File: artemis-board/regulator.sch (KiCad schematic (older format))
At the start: 33 parts, among them Q5 AO3401A, Q6 AO3401A, Q7 2N7002, Q8 2N7002, Q9 AO3401A, U10 FP6291LR, U11 ME6210A33P, U12 ME6210A33P

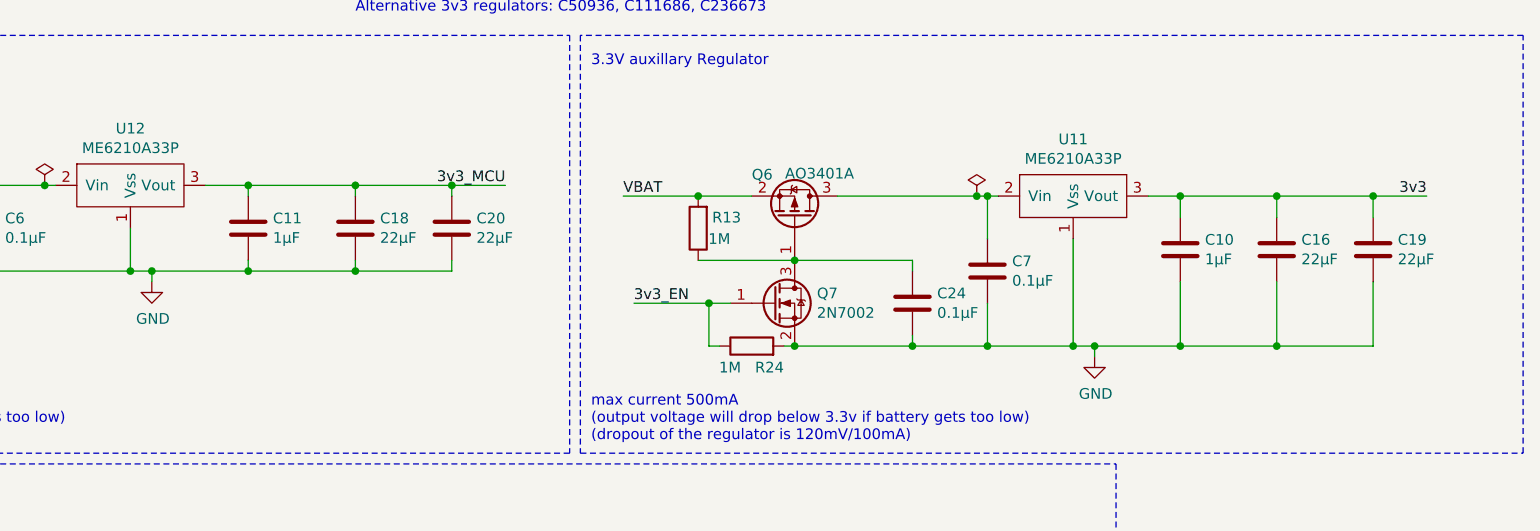
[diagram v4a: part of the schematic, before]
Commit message: removed unprotected connector, added jumper, moved cap to 3v3_mcu
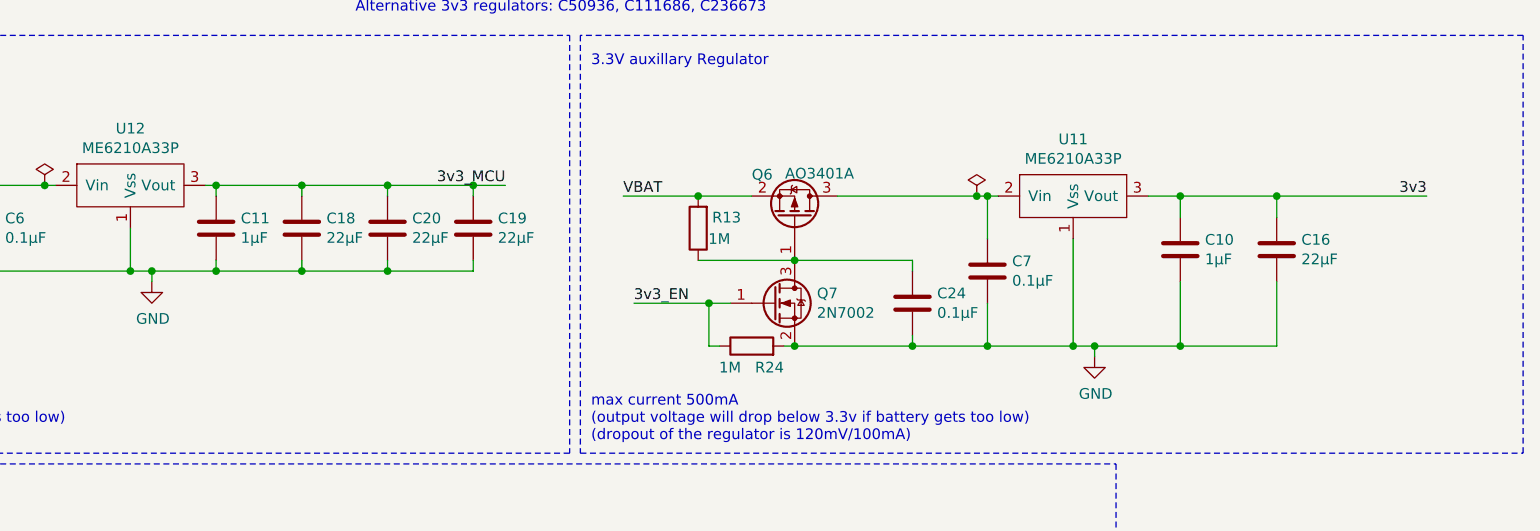
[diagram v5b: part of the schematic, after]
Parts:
- U11, U12: footprint Package_TO_SOT_SMD:SOT-89-3_Handsoldering -> Package_TO_SOT_SMD:SOT-89-3
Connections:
- net 3v3: no longer C19.1
- net 3v3_MCU: now also C19.1
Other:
- moved on the sheet: C11, C18, C20
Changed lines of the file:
@@
 VBAT
-Wire Wire Line
-	8950 3050 9400 3050
 Wire Wire Line
 	5950 3550 6300 3550
@@
 	2700 3000 2900 3000
 Wire Wire Line
-	3950 3000 4150 3000
-Wire Wire Line
-	4650 3050 4650 3000
-Connection ~ 4650 3000
-Wire Wire Line
-	4150 3050 4150 3000
-Connection ~ 4150 3000
-Wire Wire Line
-	4150 3000 4650 3000
-Wire Wire Line
-	4650 3350 4650 3400
-Wire Wire Line
-	4650 3400 4150 3400
-Wire Wire Line
-	4150 3400 4150 3350
-Connection ~ 4150 3400
+	3950 3000 4000 3000
+Wire Wire Line
+	4400 3050 4400 3000
+Wire Wire Line
+	4000 3050 4000 3000
+Wire Wire Line
+	4400 3350 4400 3400
+Wire Wire Line
+	4000 3400 4000 3350
 Connection ~ 3600 3400
 Wire Wire Line
@@
 Connection ~ 3700 3400
 Wire Wire Line
-	3700 3400 4150 3400
+	3700 3400 4000 3400
 Wire Wire Line
 	8100 3800 8100 3750
@@
 	600  600  600  2050
 Wire Wire Line
-	9400 3450 9400 3750
-Wire Wire Line
-	5100 3350 5100 3400
-Wire Wire Line
-	5100 3400 4650 3400
-Connection ~ 4650 3400
-Wire Wire Line
-	5100 3050 5100 3000
-Wire Wire Line
-	4650 3000 5100 3000
+	4800 3350 4800 3400
+Wire Wire Line
+	4800 3050 4800 3000
 Text Label 5350 3000 2    50   ~ 0
 3v3_MCU
-Wire Wire Line
-	5350 3000 5100 3000
-Connection ~ 5100 3000
-Wire Wire Line
-	8950 3750 9400 3750
-Connection ~ 8950 3750
-Wire Wire Line
-	9400 3150 9400 3050
-Connection ~ 9400 3050
-Wire Wire Line
-	9400 3050 9650 3050
 Wire Notes Line
 	1200 4300 8200 4300
@@
 L Device:C C20
 U 1 1 6037883A
-P 5100 3200
-F 0 "C20" H 5215 3246 50  0000 L CNN
-F 1 "22µF" H 5215 3155 50  0000 L CNN
-F 2 "Capacitor_SMD:C_0805_2012Metric" H 5138 3050 50  0001 C CNN
-F 3 "~" H 5100 3200 50  0001 C CNN
-F 4 "C45783" H 5100 3200 50  0001 C CNN "LCSC"
-	1    5100 3200
-	1    0    0    -1
-$EndComp
-$Comp
-L Device:C C19
-U 1 1 60374573
-P 9400 3300
-F 0 "C19" H 9515 3346 50  0000 L CNN
-F 1 "22µF" H 9515 3255 50  0000 L CNN
-F 2 "Capacitor_SMD:C_0805_2012Metric" H 9438 3150 50  0001 C CNN
-F 3 "~" H 9400 3300 50  0001 C CNN
-F 4 "C45783" H 9400 3300 50  0001 C CNN "LCSC"
-	1    9400 3300
+P 4800 3200
+F 0 "C20" H 4915 3246 50  0000 L CNN
+F 1 "22µF" H 4915 3155 50  0000 L CNN
+F 2 "Capacitor_SMD:C_0805_2012Metric" H 4838 3050 50  0001 C CNN
+F 3 "~" H 4800 3200 50  0001 C CNN
+F 4 "C45783" H 4800 3200 50  0001 C CNN "LCSC"
+	1    4800 3200
 	1    0    0    -1
 $EndComp
@@
 F 0 "U12" H 3600 3265 50  0000 C CNN
 F 1 "ME6210A33P" H 3600 3174 50  0000 C CNN
-F 2 "Package_TO_SOT_SMD:SOT-89-3_Handsoldering" H 3600 3450 50  0001 C CNN
+F 2 "Package_TO_SOT_SMD:SOT-89-3" H 3600 3450 50  0001 C CNN
 F 3 "https://datasheet.lcsc.com/szlcsc/1810201611_MICRONE-Nanjing-Micro-One-Elec-ME6210A33PG_C85233.pdf" H 3600 3450 50  0001 C CNN
 F 4 "C85233" H 3600 3550 50  0001 C CNN "LCSC"
@@
 L Device:C C18
 U 1 1 5F87C4EA
-P 4650 3200
-F 0 "C18" H 4765 3246 50  0000 L CNN
-F 1 "22µF" H 4765 3155 50  0000 L CNN
-F 2 "Capacitor_SMD:C_0805_2012Metric" H 4688 3050 50  0001 C CNN
-F 3 "~" H 4650 3200 50  0001 C CNN
-F 4 "C45783" H 4650 3200 50  0001 C CNN "LCSC"
-	1    4650 3200
+P 4400 3200
+F 0 "C18" H 4515 3246 50  0000 L CNN
+F 1 "22µF" H 4515 3155 50  0000 L CNN
+F 2 "Capacitor_SMD:C_0805_2012Metric" H 4438 3050 50  0001 C CNN
+F 3 "~" H 4400 3200 50  0001 C CNN
+F 4 "C45783" H 4400 3200 50  0001 C CNN "LCSC"
+	1    4400 3200
 	1    0    0    -1
 $EndComp
@@
 L Device:C C11
 U 1 1 5F822A09
-P 4150 3200
-F 0 "C11" H 4265 3246 50  0000 L CNN
-F 1 "1µF" H 4265 3155 50  0000 L CNN
-F 2 "Capacitor_SMD:C_0603_1608Metric_Pad1.08x0.95mm_HandSolder" H 4188 3050 50  0001 C CNN
-F 3 "~" H 4150 3200 50  0001 C CNN
-F 4 "C15849" H 4150 3200 50  0001 C CNN "LCSC"
-	1    4150 3200
+P 4000 3200
+F 0 "C11" H 4115 3246 50  0000 L CNN
+F 1 "1µF" H 4115 3155 50  0000 L CNN
+F 2 "Capacitor_SMD:C_0603_1608Metric_Pad1.08x0.95mm_HandSolder" H 4038 3050 50  0001 C CNN
+F 3 "~" H 4000 3200 50  0001 C CNN
+F 4 "C15849" H 4000 3200 50  0001 C CNN "LCSC"
+	1    4000 3200
 	1    0    0    -1
 $EndComp
@@
 F 0 "U11" H 8000 3315 50  0000 C CNN
 F 1 "ME6210A33P" H 8000 3224 50  0000 C CNN
-F 2 "Package_TO_SOT_SMD:SOT-89-3_Handsoldering" H 8000 3500 50  0001 C CNN
+F 2 "Package_TO_SOT_SMD:SOT-89-3" H 8000 3500 50  0001 C CNN
 F 3 "https://datasheet.lcsc.com/szlcsc/1810201611_MICRONE-Nanjing-Micro-One-Elec-ME6210A33PG_C85233.pdf" H 8000 3500 50  0001 C CNN
 F 4 "C85233" H 8000 3600 50  0001 C CNN "LCSC"
@@
 	6650 3750 6700 3750
 Connection ~ 6700 3750
+$Comp
+L Device:C C19
+U 1 1 60ED208A
+P 5200 3200
+F 0 "C19" H 5315 3246 50  0000 L CNN
+F 1 "22µF" H 5315 3155 50  0000 L CNN
+F 2 "Capacitor_SMD:C_0805_2012Metric" H 5238 3050 50  0001 C CNN
+F 3 "~" H 5200 3200 50  0001 C CNN
+F 4 "C45783" H 5200 3200 50  0001 C CNN "LCSC"
+	1    5200 3200
+	1    0    0    -1
+$EndComp
+Connection ~ 4000 3000
+Connection ~ 4000 3400
+Connection ~ 4400 3000
+Connection ~ 4400 3400
+Connection ~ 4800 3000
+Connection ~ 4800 3400
+Wire Wire Line
+	4000 3000 4400 3000
+Wire Wire Line
+	4400 3400 4800 3400
+Wire Wire Line
+	4400 3000 4800 3000
+Wire Wire Line
+	4800 3000 5200 3000
+Wire Wire Line
+	4000 3400 4400 3400
+Wire Wire Line
+	5200 3400 5200 3350
+Wire Wire Line
+	4800 3400 5200 3400
+Wire Wire Line
+	5200 3050 5200 3000
+Connection ~ 5200 3000
+Wire Wire Line
+	5200 3000 5350 3000
+Wire Wire Line
+	8950 3050 9650 3050
 $EndSCHEMATC

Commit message: added cap to 3v3 I2c, swapped some footprints to normal...
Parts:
- U10: footprint Package_TO_SOT_SMD:SOT-23-6_Handsoldering -> Package_TO_SOT_SMD:SOT-23-6
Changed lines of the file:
@@
 F 0 "U10" H 3650 5500 50  0000 C CNN
 F 1 "FP6291LR" H 3950 5500 50  0000 C CNN
-F 2 "Package_TO_SOT_SMD:SOT-23-6_Handsoldering" H 3850 5600 50  0001 C CNN
+F 2 "Package_TO_SOT_SMD:SOT-23-6" H 3850 5600 50  0001 C CNN
 F 3 "www.feeling-tech.com.tw/km-master/ezcatfiles/cust/img/img/24/fp6291v064.pdf" H 3850 5400 50  0001 C CNN
 F 4 "C18701" H 3850 5700 50  0001 C CNN "LCSC"

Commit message: added comments, part numbers and extended marker
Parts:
- L1, U10, U11, U12: Extended (none) -> Extended
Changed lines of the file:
@@
 F 3 "https://datasheet.lcsc.com/szlcsc/1811091611_Sunltech-Tech-SLO0630H6R8MTT_C207841.pdf" H 3850 4900 50  0001 C CNN
 F 4 "C207841" H 3850 4900 50  0001 C CNN "LCSC"
+F 5 "Extended" H 3850 4900 50  0001 C CNN "Extended"
 	1    3850 4900
 	0    -1   -1   0
@@
 F 3 "www.feeling-tech.com.tw/km-master/ezcatfiles/cust/img/img/24/fp6291v064.pdf" H 3850 5400 50  0001 C CNN
 F 4 "C18701" H 3850 5700 50  0001 C CNN "LCSC"
+F 5 "Extended" H 3850 5250 50  0001 C CNN "Extended"
 	1    3850 5250
 	-1   0    0    -1
@@
 F 3 "https://datasheet.lcsc.com/szlcsc/1810201611_MICRONE-Nanjing-Micro-One-Elec-ME6210A33PG_C85233.pdf" H 3600 3450 50  0001 C CNN
 F 4 "C85233" H 3600 3550 50  0001 C CNN "LCSC"
+F 5 "Extended" H 3600 3000 50  0001 C CNN "Extended"
 	1    3600 3000
 	1    0    0    -1
@@
 F 3 "https://datasheet.lcsc.com/szlcsc/1810201611_MICRONE-Nanjing-Micro-One-Elec-ME6210A33PG_C85233.pdf" H 8000 3500 50  0001 C CNN
 F 4 "C85233" H 8000 3600 50  0001 C CNN "LCSC"
+F 5 "Extended" H 8000 3050 50  0001 C CNN "Extended"
 	1    8000 3050
 	1    0    0    -1
